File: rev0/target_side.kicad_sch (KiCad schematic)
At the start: 12 parts, among them IC1 ECP5-BGA256, U9 USB3343-CP

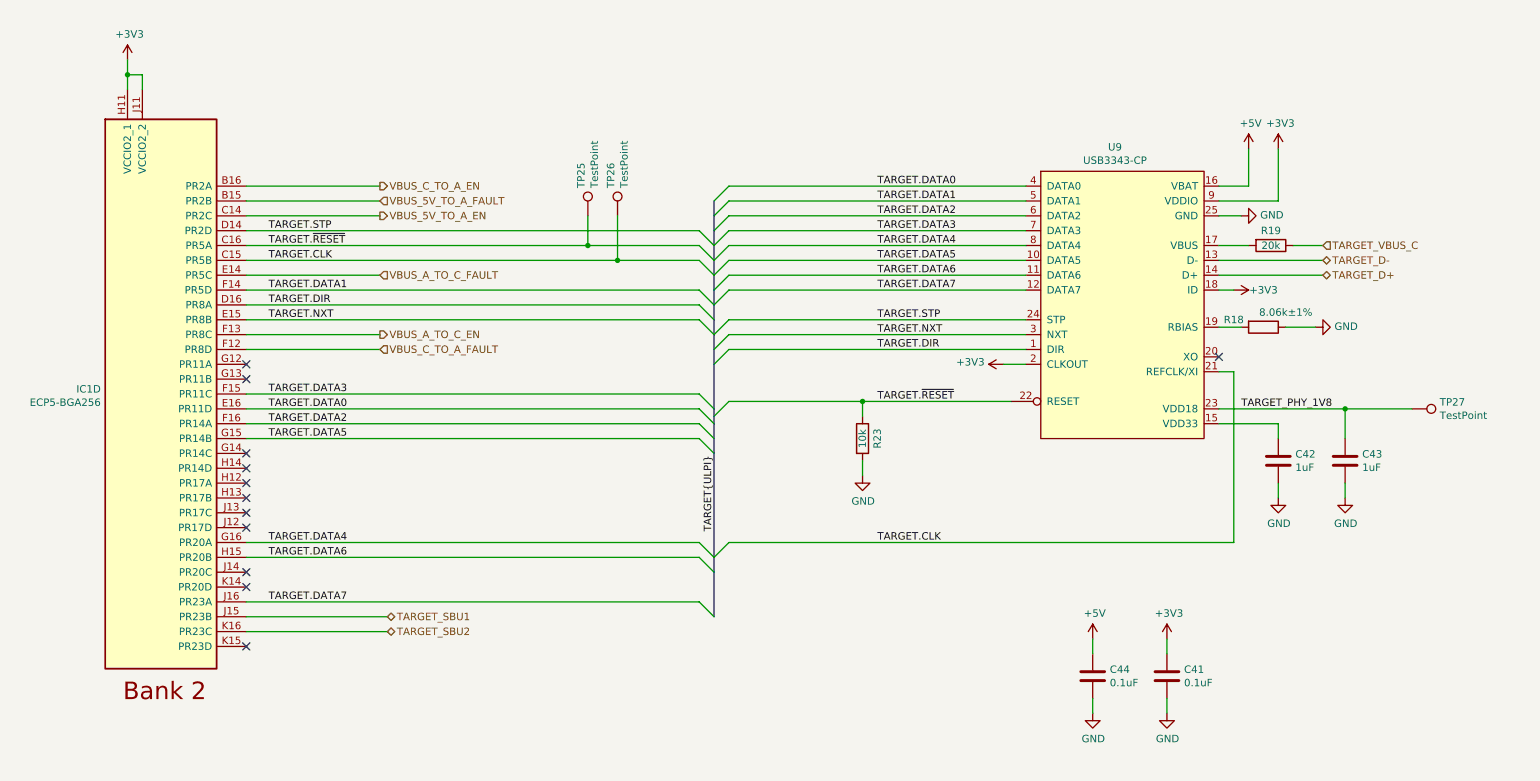
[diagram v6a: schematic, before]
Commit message: hardware: reassign FPGA I/O banks
assign HyperRAM to DQS group
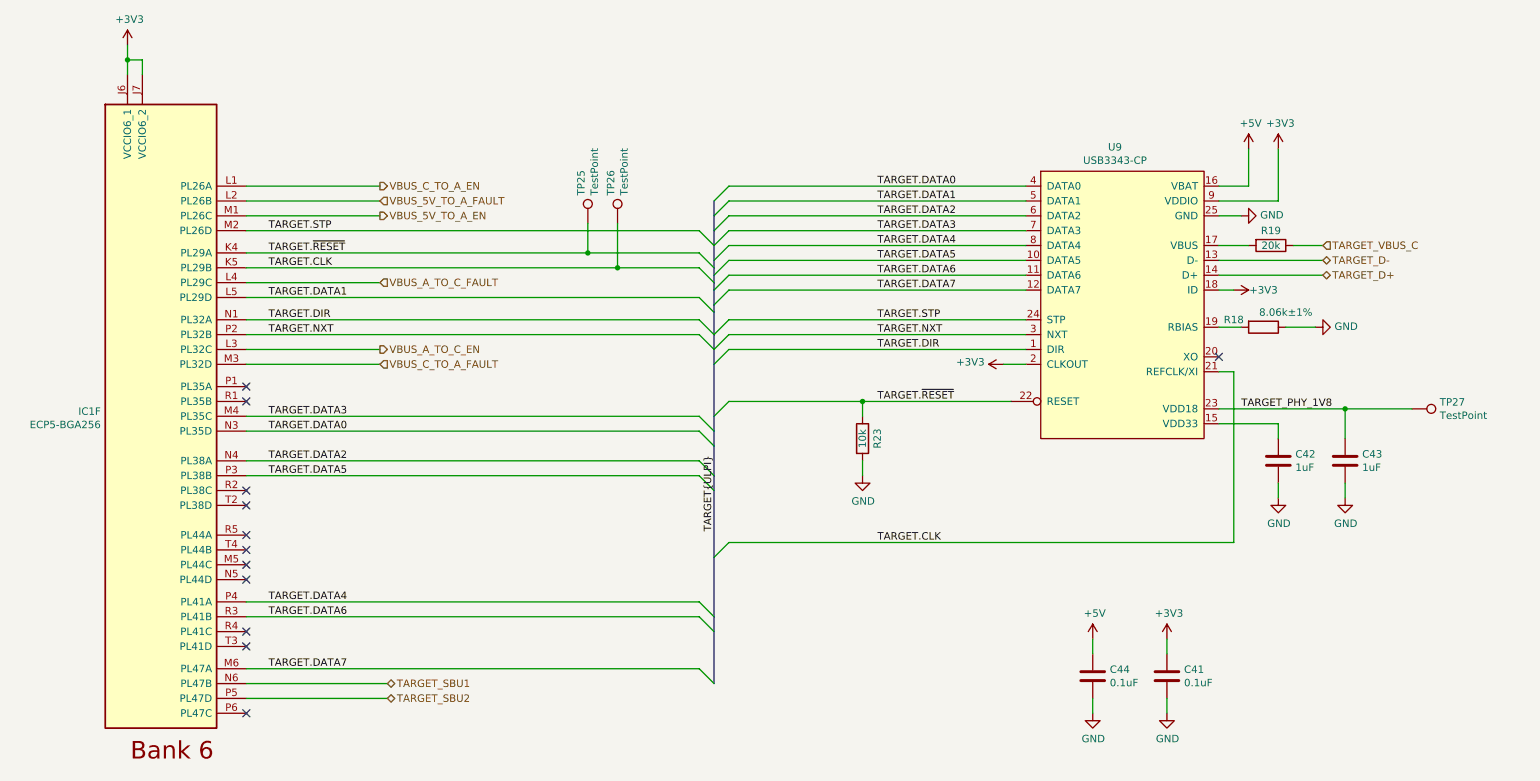
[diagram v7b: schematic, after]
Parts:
- removed IC1: ECP5-BGA256, luna:lattice_cabga256, symbol fpgas_and_processors:ECP5-BGA256
- added IC1: ECP5-BGA256, luna:lattice_cabga256, symbol fpgas_and_processors:ECP5-BGA256
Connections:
- net +3V3: now also IC1.J6 (VCCIO6_1), IC1.J7 (VCCIO6_2)
- net TARGET.CLK: now also IC1.K5 (PL29B)
- net TARGET.DATA0: now also IC1.N3 (PL35D)
- net TARGET.DATA1: now also IC1.L5 (PL29D)
- net TARGET.DATA2: now also IC1.N4 (PL38A)
- net TARGET.DATA3: now also IC1.M4 (PL35C)
- net TARGET.DATA4: now also IC1.P4 (PL41A)
- net TARGET.DATA5: now also IC1.P3 (PL38B)
- net TARGET.DATA6: now also IC1.R3 (PL41B)
- net TARGET.DATA7: now also IC1.M6 (PL47A)
- net TARGET.DIR: now also IC1.N1 (PL32A)
- net TARGET.NXT: now also IC1.P2 (PL32B)
- net TARGET.STP: now also IC1.M2 (PL26D)
- net TARGET.~{RESET}: now also IC1.K4 (PL29A)
- net TARGET_SBU1: now also IC1.N6 (PL47B)
- net TARGET_SBU2: now also IC1.P5 (PL47D)
- net VBUS_5V_TO_A_EN: now also IC1.M1 (PL26C)
- net VBUS_5V_TO_A_FAULT: now also IC1.L2 (PL26B)
- net VBUS_A_TO_C_EN: now also IC1.L3 (PL32C)
- net VBUS_A_TO_C_FAULT: now also IC1.L4 (PL29C)
- net VBUS_C_TO_A_EN: now also IC1.L1 (PL26A)
- net VBUS_C_TO_A_FAULT: now also IC1.M3 (PL32D)
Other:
- moved on the sheet: TP25, TP26

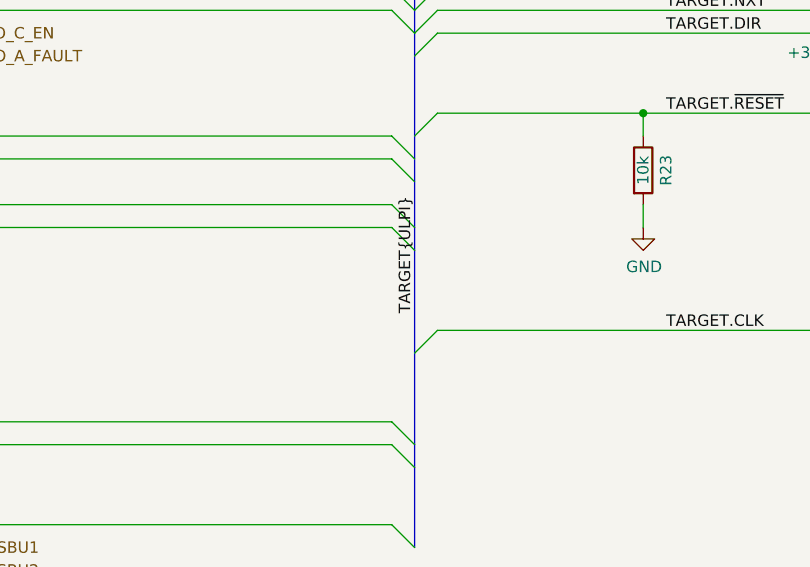
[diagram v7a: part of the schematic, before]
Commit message: hardware: rename USB ports
Sideband is renamed to Control and is intended for use as the primary
control port for both the FPGA and the microcontroller/debugger.

Host is renamed to Aux and is intended for auxiliary functions
including MitM.
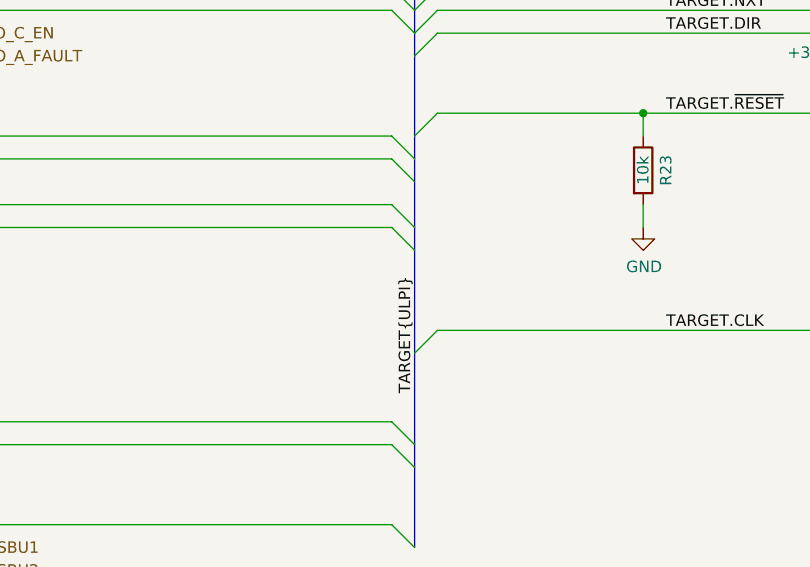
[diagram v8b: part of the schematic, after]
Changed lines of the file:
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@@
     (effects (font (size 1.27 1.27)) (justify left bottom))
   )
-  (label "TARGET{ULPI}" (at 139.7 112.395 90)
+  (label "TARGET{ULPI}" (at 139.7 121.285 90)
     (effects (font (size 1.27 1.27)) (justify left bottom))
   )
